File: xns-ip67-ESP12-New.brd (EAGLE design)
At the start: 65.3 x 132.3 mm, 75 parts, among them J1 DCJ0202, J24 5V, X1 ESP-12E

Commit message: Board dimension changes
Adjusted to be edge to edge
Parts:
- removed DC1: R-78C1.8-1.0, dc-dc-converter:SIP3
- added DC3V3: R-78C1.8-1.0, dc-dc-converter:SIP3
- moved U1 17.7 mm to (52.1, 22.9)
- moved J17 9.92 mm to (64.8, 27.9)
- moved J18 9.92 mm to (11.4, 53.3)
- moved J21 9.92 mm to (49.5, 53.3)
- moved J30 9.92 mm to (39.4, 67.3)
- moved J7 9.92 mm to (49.5, 33.0)
- moved JP1 9.92 mm to (25.4, 108.0)
- moved JP10 9.92 mm to (25.4, 85.1)
- moved JP12 9.92 mm to (25.4, 80.0)
- moved JP13 9.92 mm to (25.4, 77.5)
- moved JP14 9.92 mm to (25.4, 74.9)
- moved JP15 9.92 mm to (25.4, 72.4)
- moved JP16 9.92 mm to (48.3, 72.4)
- moved JP17 9.92 mm to (48.3, 74.9)
- moved JP18 9.92 mm to (48.3, 77.5)
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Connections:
- net GND: now also DC3V3.2; no longer DC1.2
- net VCC: now also DC3V3.1; no longer DC1.1
- net VDD: now also DC3V3.3; no longer DC1.3
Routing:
- net VDD: track 0.00 -> 265.0 mm
- net VCC: track 0.00 -> 48.0 mm
- net N$2: track 0.00 -> 20.3 mm
- net N$11: track 0.00 -> 20.2 mm
- net N$50: track 0.00 -> 19.7 mm
- net N$33: track 0.00 -> 19.7 mm
- net N$27: track 0.00 -> 19.7 mm
- net N$24: track 0.00 -> 19.7 mm
- net N$51: track 0.00 -> 19.7 mm
- net N$47: track 0.00 -> 19.7 mm
- net N$42: track 0.00 -> 19.7 mm
- net N$39: track 0.00 -> 19.7 mm
- net N$44: track 0.00 -> 19.7 mm
- net N$36: track 0.00 -> 19.7 mm
- net N$30: track 0.00 -> 19.7 mm
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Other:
- board size 65.3 x 132.3 mm -> 65.3 x 139.1 mm
- board text added: "CH"
- board text removed: "CHPD"

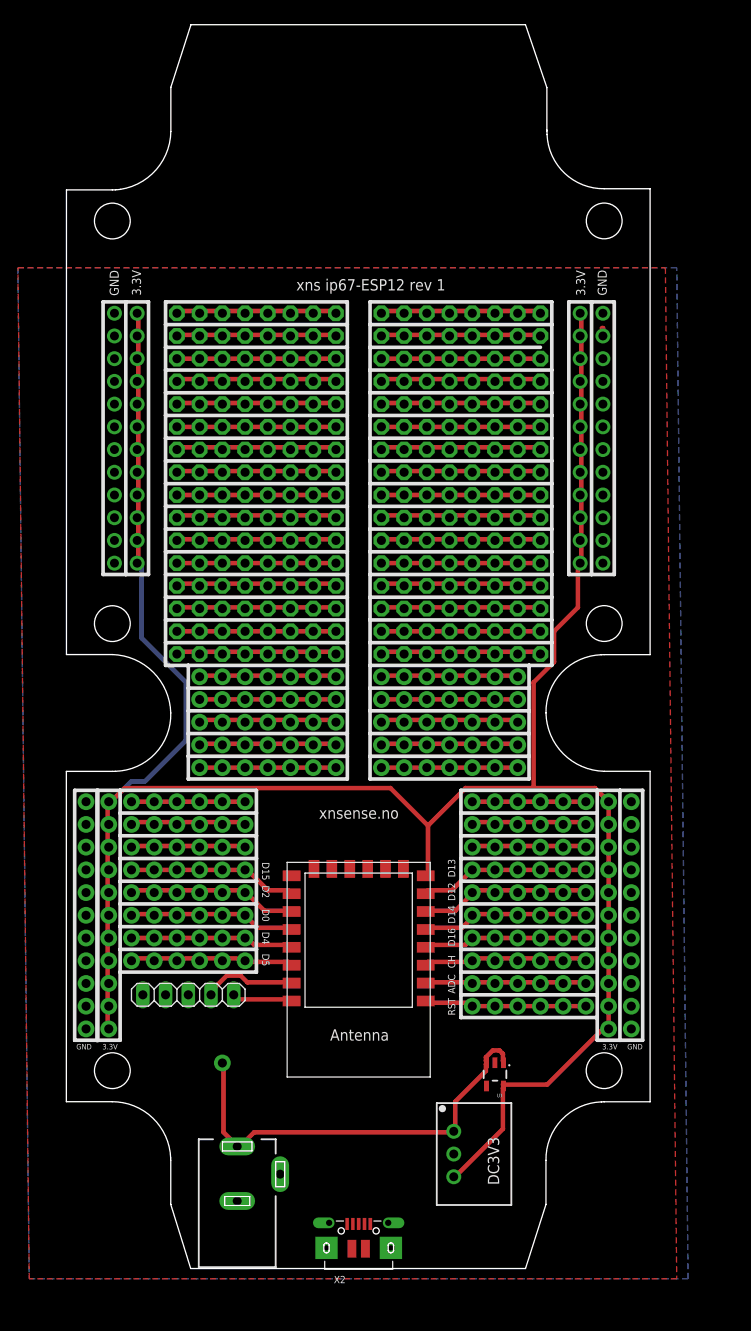
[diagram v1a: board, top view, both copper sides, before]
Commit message: Added LiPo charging (new)
Components are not aligned etc, just added based on feather board. No
other components has been removed.
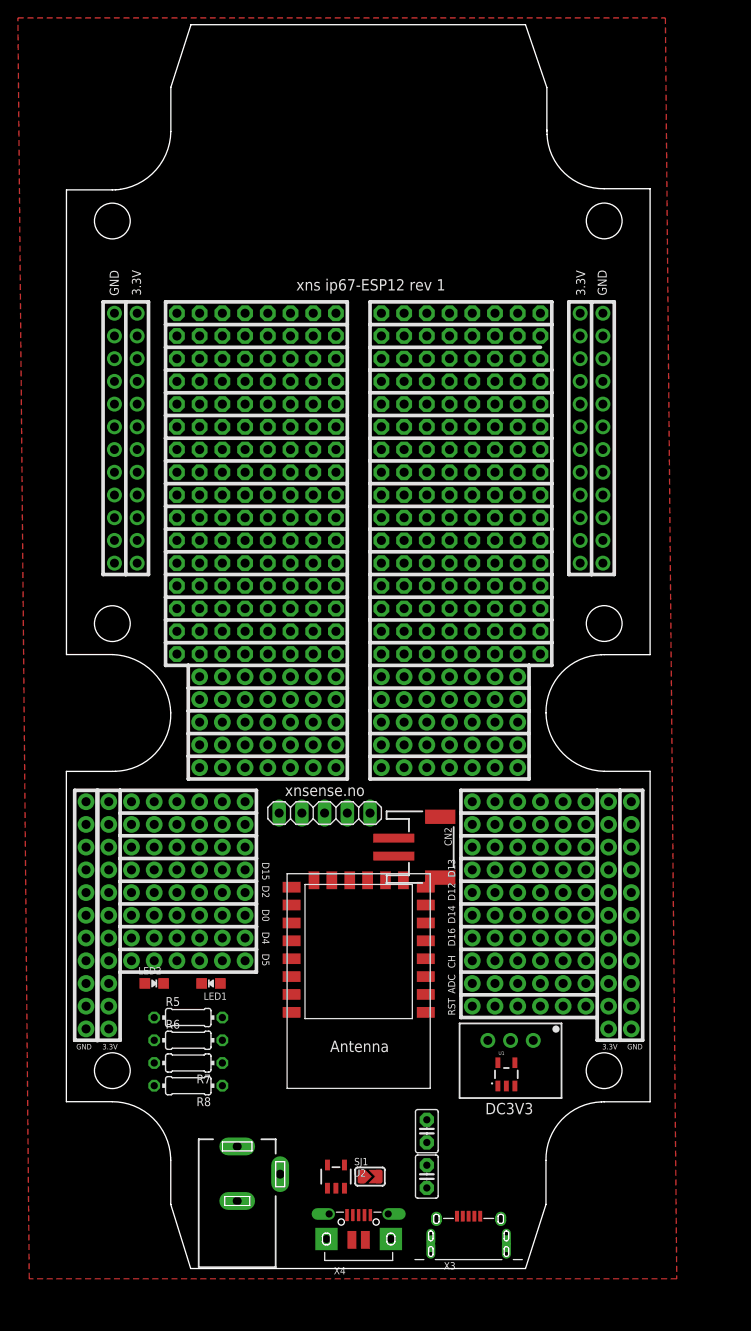
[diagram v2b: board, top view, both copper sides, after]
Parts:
- removed J24: 5V, SparkFun-Connectors:1X01_NO_SILK
- removed X2: (no value), microbuilder:4UCONN_20329
- added C3, C4: 10uF, capacitor-wima:C2.5-2
- added CN2: JSTPH, microbuilder:JSTPH2
- added LED1: RED, microbuilder:CHIPLED_0805_NOOUTLINE
- added LED2: GREEN, microbuilder:CHIPLED_0805_NOOUTLINE
- added R5, R6: 470, eagle-ltspice:0204/7
- added R7: 10k, eagle-ltspice:0204/7
- added R8: 2.5k, eagle-ltspice:0204/7
- added SJ1: (no value), microbuilder:SOLDERJUMPER_ARROW_NOPASTE
- added U2: MCP73831T-2ACI/OT, microbuilder:SOT23-5
- added X3: (no value), jcbrataas:USB-MICRO-B
- added X4: (no value), microbuilder:4UCONN_20329_V2
- moved JP37 25.4 mm to (33.0, 52.1)
- moved DC3V3 14.2 mm to (53.8, 26.6), turned to 180 degrees
- moved U1 1.27 mm to (53.3, 22.9), turned to 0 degrees
- moved X1 1.27 mm to (36.8, 35.6)
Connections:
- new net N$53: LED1.C, R5.1
- new net N$55: R5.2, R6.2, U2.1
- new net N$57: R7.1, SJ1.2, U2.5
- new net N$59: LED2.A, R6.1
- new net N$60: R8.1, SJ1.1
- new net VBAT1: C4.1, CN2.2, U2.3
- new net VDD1: C3.1, LED1.A, U2.4, X4.VBUS
- net GND: now also C3.2, C4.2, CN2.1, LED2.C, R7.2, R8.2, U2.2, X3.BL1, X3.BL2, X3.BL3, X3.BR1, X3.BR2, X3.BR3, X3.GND, X3.MTL1, X3.MTL2, X3.MTR1, X3.MTR2, X4.BASE@1, X4.BASE@2, X4.GND, X4.SPRT@1, X4.SPRT@2, X4.SPRT@3, X4.SPRT@4; no longer X2.BASE@1, X2.BASE@2, X2.GND, X2.SPRT@1, X2.SPRT@2, X2.SPRT@3, X2.SPRT@4
- net VCC: now also X3.VBUS; no longer J24.1, X2.VBUS
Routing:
- net VDD: track 265.0 -> 0.00 mm
- net VCC: track 48.0 -> 0.00 mm
- net N$2: track 20.3 -> 0.00 mm
- net N$11: track 20.2 -> 0.00 mm
- net N$50: track 19.7 -> 0.00 mm
- net N$33: track 19.7 -> 0.00 mm
- net N$27: track 19.7 -> 0.00 mm
- net N$24: track 19.7 -> 0.00 mm
- net N$51: track 19.7 -> 0.00 mm
- net N$47: track 19.7 -> 0.00 mm
- net N$42: track 19.7 -> 0.00 mm
- net N$39: track 19.7 -> 0.00 mm
- net N$44: track 19.7 -> 0.00 mm
- net N$36: track 19.7 -> 0.00 mm
- net N$30: track 19.7 -> 0.00 mm
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- removed copper zone on layer 16, net GND
